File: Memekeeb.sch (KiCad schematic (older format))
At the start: 80 parts, among them K1 KEYSW, K10 KEYSW, K11 KEYSW, K12 KEYSW, K14 KEYSW, K15 KEYSW, K16 KEYSW, K17 KEYSW, K18 KEYSW, K19 KEYSW, K2 KEYSW, K20 KEYSW, K21 KEYSW, K22 KEYSW, K23 KEYSW, K24 KEYSW, K25 KEYSW, K27 KEYSW, K28 KEYSW, K29 KEYSW, K3 KEYSW, K30 KEYSW, K31 KEYSW, K32 KEYSW, K33 KEYSW, K34 KEYSW, K35 KEYSW, K36 KEYSW, K37 KEYSW, K4 KEYSW, K5 KEYSW, K6 KEYSW, K7 KEYSW, K8 KEYSW, K9 KEYSW

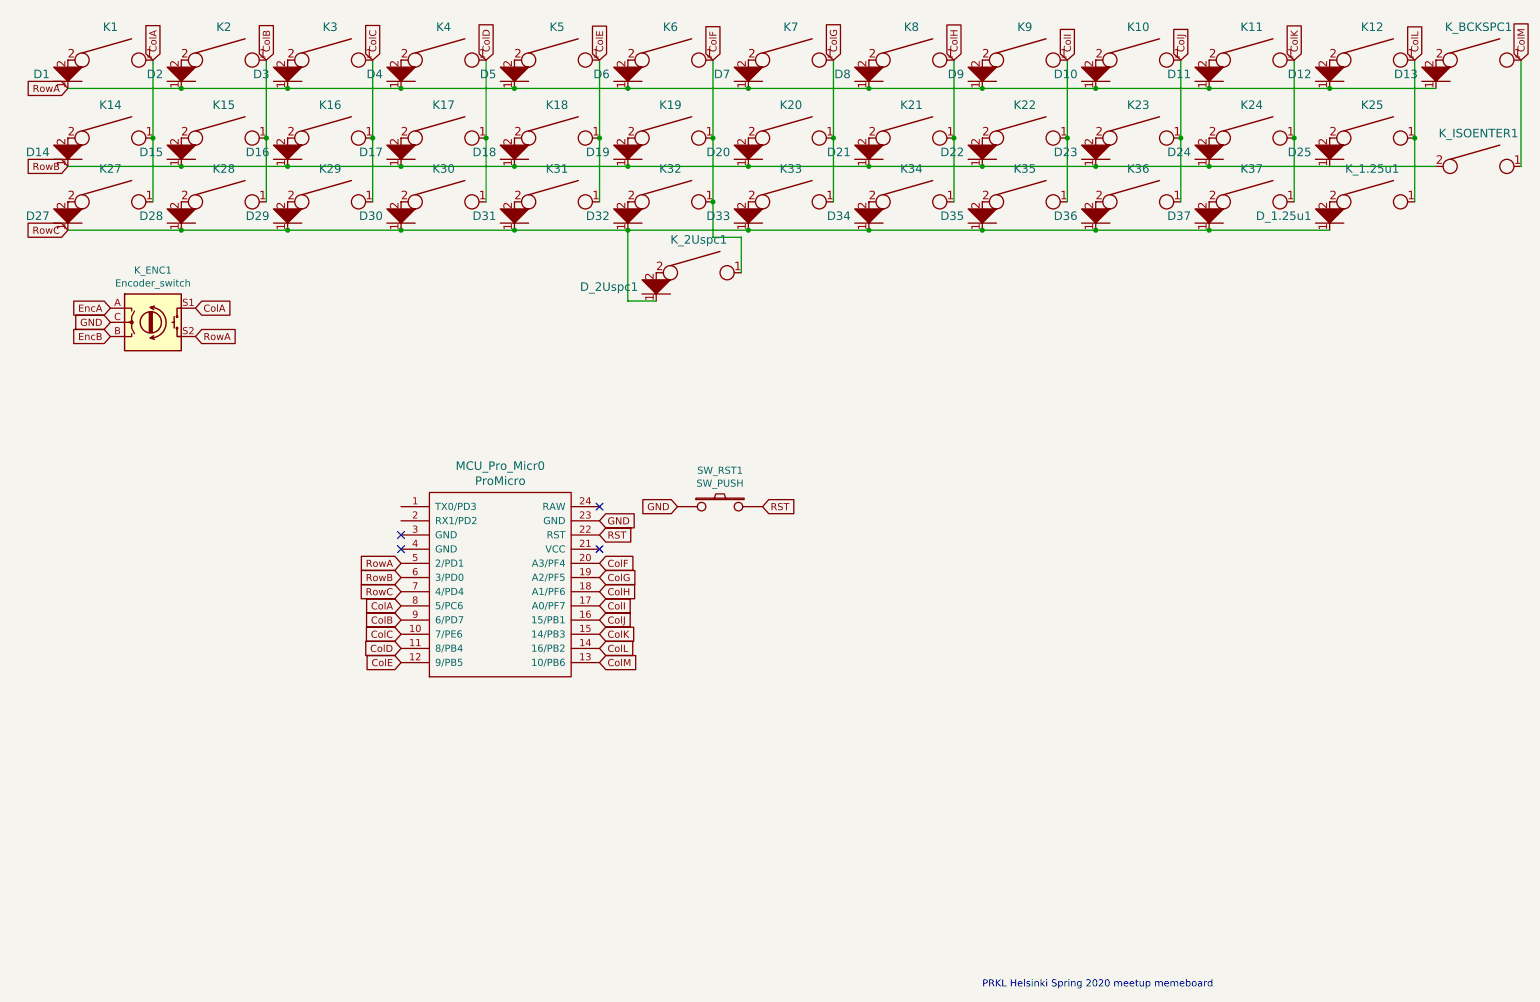
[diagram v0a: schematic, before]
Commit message: Add WS2812B LED Strip support
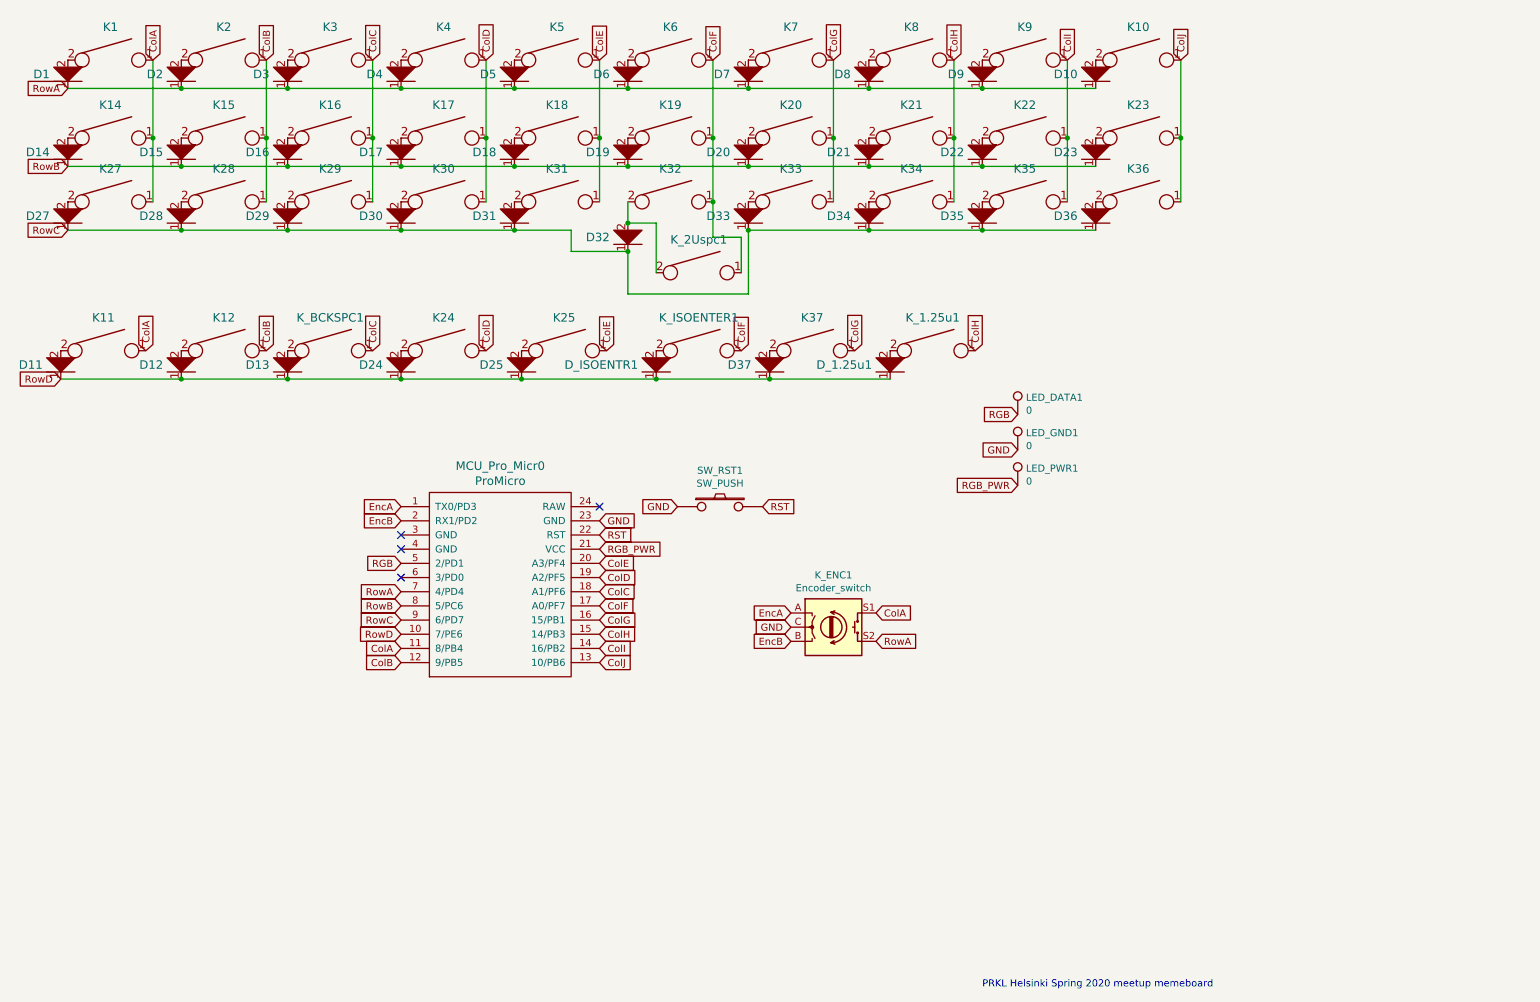
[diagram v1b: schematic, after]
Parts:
- removed D_2Uspc1: D, keyboard_parts:D_SOD123_axial, symbol keyboard_parts:D
- added D_ISOENTR1: D, keyboard_parts:D_SOD123_axial, symbol keyboard_parts:D
- added LED_DATA1, LED_GND1, LED_PWR1: 0, Keebio-Parts:SinglePad, symbol Connector:TestPoint
- K1, K10, K11, K12, K14, K15, K16, K17, K18, K19, K2, K20, K21, K22, K23, K24, K25, K27, K28, K29, K3, K30, K31, K32, K33, K34, K35, K36, K37, K4, K5, K6, K7, K8, K9: footprint Keebio-Parts:MX-Alps-Choc-1U -> Keebio-Parts:MX-Alps-Choc-1U-NoLED
- K_1.25u1: footprint Button_Switch_Keyboard:SW_Cherry_MX1A_1.25u_PCB -> Keebio-Parts:MX-Alps-Choc-1U-NoLED
- K_BCKSPC1: footprint Keebio-Parts:MX_PCB_150H -> Keebio-Parts:MX-Alps-Choc-1U-NoLED
- K_ISOENTER1: footprint Button_Switch_Keyboard:SW_Cherry_MX1A_ISOEnter_Plate -> Keebio-Parts:MX-Alps-Choc-2U
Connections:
- net ColA: now also K11.1, MCU_Pro_Micr0.11 (8/PB4); no longer MCU_Pro_Micr0.8 (5/PC6)
- net ColB: now also K12.1, MCU_Pro_Micr0.12 (9/PB5); no longer MCU_Pro_Micr0.9 (6/PD7)
- net ColC: now also K_BCKSPC1.1, MCU_Pro_Micr0.18 (A1/PF6); no longer MCU_Pro_Micr0.10 (7/PE6)
- net ColD: now also K24.1, MCU_Pro_Micr0.19 (A2/PF5); no longer MCU_Pro_Micr0.11 (8/PB4)
- net ColE: now also K25.1, MCU_Pro_Micr0.20 (A3/PF4); no longer MCU_Pro_Micr0.12 (9/PB5)
- net ColF: now also K_ISOENTER1.1, MCU_Pro_Micr0.17 (A0/PF7); no longer MCU_Pro_Micr0.20 (A3/PF4)
- net ColG: now also K37.1, MCU_Pro_Micr0.16 (15/PB1); no longer MCU_Pro_Micr0.19 (A2/PF5)
- net ColH: now also K_1.25u1.1, MCU_Pro_Micr0.15 (14/PB3); no longer MCU_Pro_Micr0.18 (A1/PF6)
- net ColI: now also MCU_Pro_Micr0.14 (16/PB2); no longer MCU_Pro_Micr0.17 (A0/PF7)
- net ColJ: now also MCU_Pro_Micr0.13 (10/PB6); no longer MCU_Pro_Micr0.16 (15/PB1)
- net EncA: now also MCU_Pro_Micr0.1 (TX0/PD3)
- net EncB: now also MCU_Pro_Micr0.2 (RX1/PD2)
- net GND: now also LED_GND1.1
- net RowA: now also MCU_Pro_Micr0.7 (4/PD4); no longer D11.1, D12.1, D13.1, MCU_Pro_Micr0.5 (2/PD1)
- net RowB: now also MCU_Pro_Micr0.8 (5/PC6); no longer D24.1, D25.1, K_ISOENTER1.2, MCU_Pro_Micr0.6 (3/PD0)
- net RowC: now also MCU_Pro_Micr0.9 (6/PD7); no longer D37.1, D_1.25u1.1, MCU_Pro_Micr0.7 (4/PD4)
- net at D32.2, K32.2: now also K_2Uspc1.2
- net RGB_PWR: now reaches MCU_Pro_Micr0.21 (VCC)
- net RGB_PWR: now also LED_PWR1.1
- removed net ColK: K11.1, K24.1, K37.1, MCU_Pro_Micr0.15 (14/PB3)
- removed net ColL: K12.1, K25.1, K_1.25u1.1, MCU_Pro_Micr0.14 (16/PB2)
- removed net ColM: K_BCKSPC1.1, K_ISOENTER1.1, MCU_Pro_Micr0.13 (10/PB6)
- new net: D_ISOENTR1.2, K_ISOENTER1.2
- new net RGB: LED_DATA1.1, MCU_Pro_Micr0.5 (2/PD1)
- new net RowD: D11.1, D12.1, D13.1, D24.1, D25.1, D37.1, D_1.25u1.1, D_ISOENTR1.1, MCU_Pro_Micr0.10 (7/PE6)
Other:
- moved on the sheet: D11, D12, D13, D24, D25, D32, D37, D_1.25u1, K11, K12, K24, K25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
